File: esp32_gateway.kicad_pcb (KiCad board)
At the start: 2 copper layers, 79 parts, among them J1 POWER Int, J10 IRF, J11 Conn_01x01_Female, J12 Conn_01x01_Female, J13 Conn_01x01_Female, J14 Conn_01x01_Female, J15 Conn_01x01_Female, J16 Conn_01x01_Female, J17 Conn_01x01_Female, J18 Conn_01x01_Female, J19 Conn_01x01_Female, J2 POWER Out, J20 CC2530_B, J21 CC2530_A, J22 Conn_01x01_Female, J23 Conn_01x01_Female, J3 Conn_01x01_Female, J4 Conn_01x01_Female, J5 Uart, J6 Boot, J7 SRX882, J8 STX882, J9 Conn_01x01_Female, Q1 DMP4051LK3, Q2 BC847, Q3 BSS138, Q4 2N7002, Q5 2N7002, SW1 Reset, U1 LM1117-3.3, U2 ESP32-S

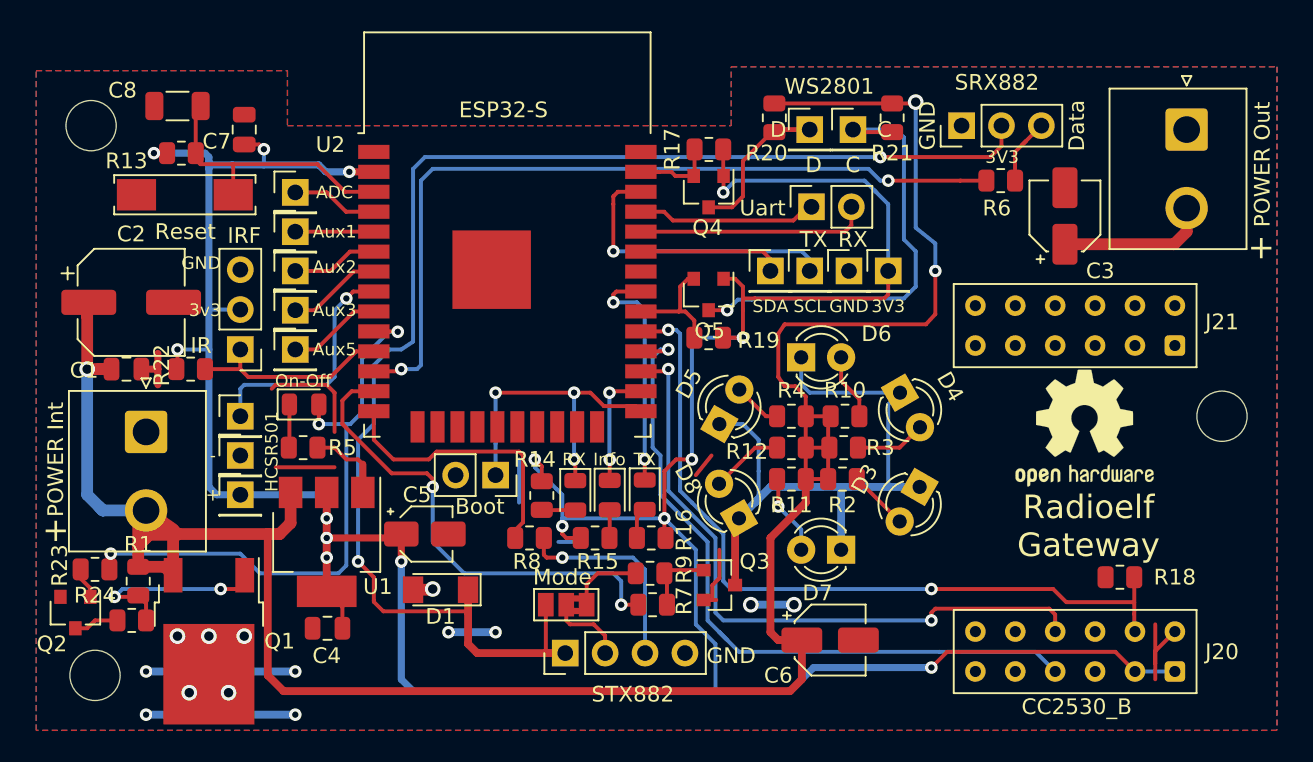
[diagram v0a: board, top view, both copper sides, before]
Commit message: Fixed errors in RF modules connection
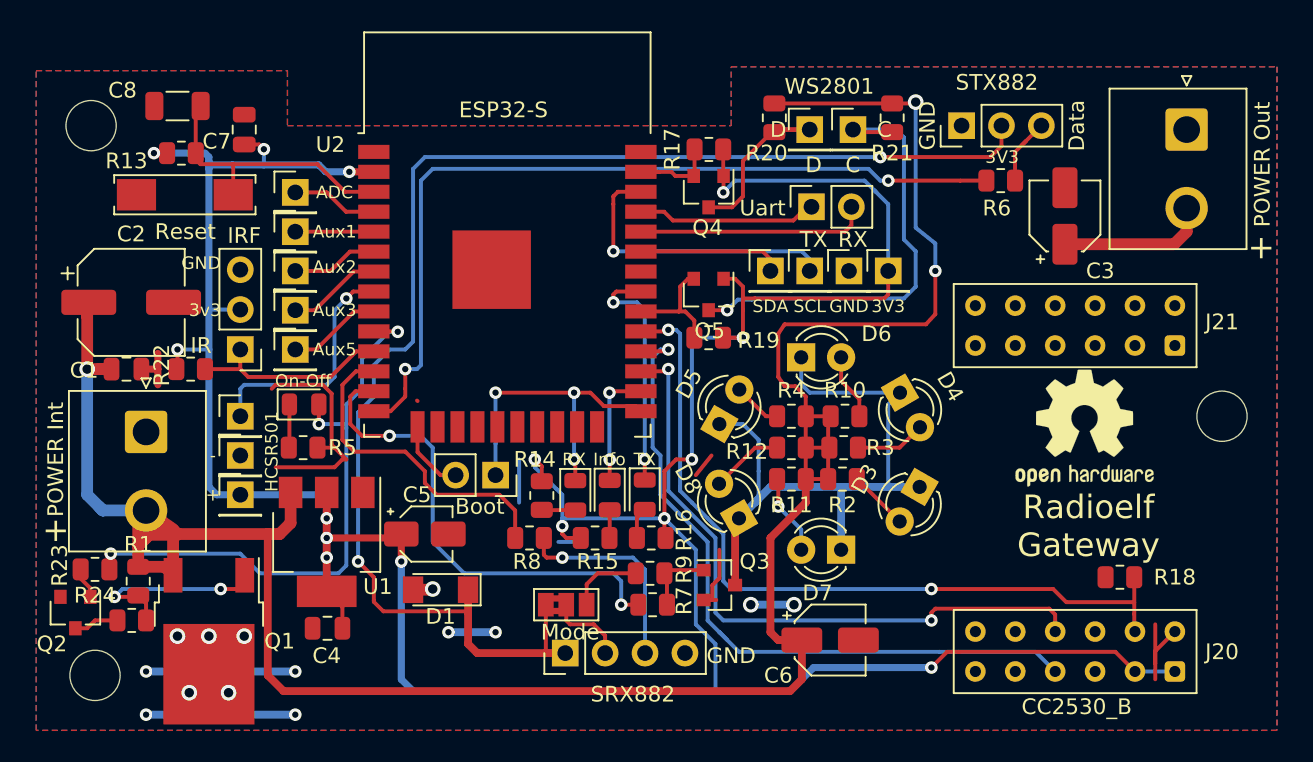
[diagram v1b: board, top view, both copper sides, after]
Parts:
- J7: value SRX882 -> STX882
- J8: value STX882 -> SRX882
- turned JP1 to 0 degrees
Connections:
- JP1 pad 1: GND -> Net-(D1-Pad1)
- JP1 pad 3: Net-(D1-Pad1) -> GND
- U2 pad 12: /RX_RF -> /TX_RF
- U2 pad 14: /TX_RF -> /RX_RF
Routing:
- net GND: track 60.2 -> 64.1 mm
- net /TX_RF: track 17.6 -> 21.4 mm
- net /RX_RF: track 51.5 -> 53.6 mm
